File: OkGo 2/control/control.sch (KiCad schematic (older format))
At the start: 49 parts, among them P101 BATT, P102 BATT, P103 BATT_CASE, P104 KEYSW, P105 KEYSW, P106 ARM_LED, P107 ARM_LED, P108 SMA, SW101 LATCHING PUSH, SW102 KEYSWITCH, U101 FUSE 1A, U102 ADP3335, U103 BEZEL, U104 LCD_HD44780, U105 STM32F071CBT6, U106 RFM95W, U107 MEU1S0303ZC, U108 SWD, Y101 8MHz

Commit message: First layout of control
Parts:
- removed TP101: BATT, common:TESTPOINT, symbol TestPoint
- removed TP103: GND, common:TESTPOINT, symbol TestPoint
- removed U101: FUSE 1A, symbol PART
- removed U107: MEU1S0303ZC, control:meu1, symbol MEU1S0303ZC
- added U101: MEJ2S0305SC, control:MEJ2S0305SC, symbol MEJ2S0305SC
- F101: value 5x20 -> PTC; footprint control:5x20_clip -> Resistors_SMD:R_0805; Farnell 1162740 -> 1294879
- U104: footprint Pin_Headers:Pin_Header_Straight_1x16 -> control:LCD_MC42004A6W; Farnell (none) -> 2342651
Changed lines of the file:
@@
 LIBS:adp3335
 LIBS:sma
-LIBS:meu1s0303zc
 LIBS:part
 LIBS:lipo_1s
@@
 LIBS:push_illum
 LIBS:push_illum_straight
+LIBS:mej2s0305sc
 LIBS:control-cache
 EELAYER 25 0
@@
 F 0 "U104" V 8250 3750 60  0000 C CNN
 F 1 "LCD_HD44780" V 8150 3750 60  0000 C CNN
-F 2 "Pin_Headers:Pin_Header_Straight_1x16" H 7450 4400 60  0001 C CNN
+F 2 "control:LCD_MC42004A6W" H 7450 4400 60  0001 C CNN
 F 3 "" H 7450 4400 60  0000 C CNN
+F 4 "2342651" H 8200 3750 60  0001 C CNN "Farnell"
 	1    8200 3750
 	1    0    0    -1
@@
 $EndComp
 $Comp
-L +BATT #PWR023
-U 1 1 55643D33
-P 7150 3550
-F 0 "#PWR023" H 7150 3400 50  0001 C CNN
-F 1 "+BATT" H 7150 3690 50  0000 C CNN
-F 2 "" H 7150 3550 60  0000 C CNN
-F 3 "" H 7150 3550 60  0000 C CNN
-	1    7150 3550
-	1    0    0    -1
-$EndComp
-$Comp
-L GND #PWR024
+L GND #PWR023
 U 1 1 55643E77
 P 7150 3650
-F 0 "#PWR024" H 7150 3400 50  0001 C CNN
+F 0 "#PWR023" H 7150 3400 50  0001 C CNN
 F 1 "GND" H 7150 3500 50  0000 C CNN
 F 2 "" H 7150 3650 60  0000 C CNN
@@
 $EndComp
 $Comp
-L GND #PWR025
+L GND #PWR024
 U 1 1 55638AFF
 P 7100 4150
-F 0 "#PWR025" H 7100 3900 50  0001 C CNN
+F 0 "#PWR024" H 7100 3900 50  0001 C CNN
 F 1 "GND" H 7100 4000 50  0000 C CNN
 F 2 "" H 7100 4150 60  0000 C CNN
@@
 $EndComp
 $Comp
-L TestPoint TP101
-U 1 1 559DAED6
-P 6700 900
-F 0 "TP101" H 6700 825 60  0000 C CNN
-F 1 "BATT" H 6700 750 60  0000 C CNN
-F 2 "common:TESTPOINT" H 6700 900 60  0001 C CNN
-F 3 "" H 6700 900 60  0000 C CNN
-	1    6700 900
-	-1   0    0    1
-$EndComp
-$Comp
-L TestPoint TP103
-U 1 1 559DAFE3
-P 6700 1000
-F 0 "TP103" H 6700 925 60  0000 C CNN
-F 1 "GND" H 6700 850 60  0000 C CNN
-F 2 "common:TESTPOINT" H 6700 1000 60  0001 C CNN
-F 3 "" H 6700 1000 60  0000 C CNN
-	1    6700 1000
-	1    0    0    -1
-$EndComp
-$Comp
 L TestPoint TP104
 U 1 1 559DB26A
@@
 $EndComp
 $Comp
-L GND #PWR026
+L GND #PWR025
 U 1 1 559E503C
 P 9000 5850
-F 0 "#PWR026" H 9000 5600 50  0001 C CNN
+F 0 "#PWR025" H 9000 5600 50  0001 C CNN
 F 1 "GND" H 9000 5700 50  0001 C CNN
 F 2 "" H 9000 5850 60  0000 C CNN
@@
 $EndComp
 $Comp
-L MEU1S0303ZC U107
-U 1 1 559EA3B4
-P 3700 6950
-F 0 "U107" H 3700 6600 60  0000 C CNN
-F 1 "MEU1S0303ZC" H 3750 6900 60  0000 C CNN
-F 2 "control:meu1" H 3700 6950 60  0001 C CNN
-F 3 "" H 3700 6950 60  0000 C CNN
-F 4 "2366449" H 3700 6950 60  0001 C CNN "Farnell"
-	1    3700 6950
-	1    0    0    -1
-$EndComp
-$Comp
-L +3V3 #PWR027
+L +3V3 #PWR026
 U 1 1 559EA6BB
 P 3150 7050
-F 0 "#PWR027" H 3150 6900 50  0001 C CNN
+F 0 "#PWR026" H 3150 6900 50  0001 C CNN
 F 1 "+3V3" H 3150 7190 50  0000 C CNN
 F 2 "" H 3150 7050 60  0000 C CNN
@@
 $EndComp
 $Comp
-L GND #PWR028
+L GND #PWR027
 U 1 1 559EA828
 P 3150 7250
-F 0 "#PWR028" H 3150 7000 50  0001 C CNN
+F 0 "#PWR027" H 3150 7000 50  0001 C CNN
 F 1 "GND" H 3150 7100 50  0000 C CNN
 F 2 "" H 3150 7250 60  0000 C CNN
@@
 $EndComp
 $Comp
-L +5V #PWR029
+L +5V #PWR028
 U 1 1 559EAA6F
 P 4350 7050
-F 0 "#PWR029" H 4350 6900 50  0001 C CNN
+F 0 "#PWR028" H 4350 6900 50  0001 C CNN
 F 1 "+5V" H 4350 7190 50  0000 C CNN
 F 2 "" H 4350 7050 60  0000 C CNN
@@
 $EndComp
 $Comp
-L GND #PWR030
+L GND #PWR029
 U 1 1 559EABE0
 P 4350 7250
-F 0 "#PWR030" H 4350 7000 50  0001 C CNN
+F 0 "#PWR029" H 4350 7000 50  0001 C CNN
 F 1 "GND" H 4350 7100 50  0000 C CNN
 F 2 "" H 4350 7250 60  0000 C CNN
@@
 P 6250 900
 F 0 "F101" H 6350 950 50  0000 C CNN
-F 1 "5x20" H 6150 850 50  0000 C CNN
-F 2 "control:5x20_clip" H 6250 900 60  0001 C CNN
+F 1 "PTC" H 6100 850 50  0000 C CNN
+F 2 "Resistors_SMD:R_0805" H 6250 900 60  0001 C CNN
 F 3 "" H 6250 900 60  0000 C CNN
-F 4 "1162740" H 6250 900 60  0001 C CNN "Farnell"
+F 4 "1294879" H 6250 900 60  0001 C CNN "Farnell"
 	1    6250 900
 	1    0    0    -1
 $EndComp
 $Comp
-L +BATT #PWR031
+L +BATT #PWR030
 U 1 1 55A7EBCE
 P 8300 900
-F 0 "#PWR031" H 8300 750 50  0001 C CNN
+F 0 "#PWR030" H 8300 750 50  0001 C CNN
 F 1 "+BATT" H 8300 1040 50  0000 C CNN
 F 2 "" H 8300 900 60  0000 C CNN
@@
 $EndComp
 $Comp
-L GND #PWR032
+L GND #PWR031
 U 1 1 55A805A4
 P 2000 1550
-F 0 "#PWR032" H 2000 1300 50  0001 C CNN
+F 0 "#PWR031" H 2000 1300 50  0001 C CNN
 F 1 "GND" H 2000 1400 50  0000 C CNN
 F 2 "" H 2000 1550 60  0000 C CNN
@@
 $EndComp
 $Comp
-L +3.3V #PWR033
+L +3.3V #PWR032
 U 1 1 55A80891
 P 2050 1000
-F 0 "#PWR033" H 2050 850 50  0001 C CNN
+F 0 "#PWR032" H 2050 850 50  0001 C CNN
 F 1 "+3.3V" H 2050 1140 50  0000 C CNN
 F 2 "" H 2050 1000 60  0000 C CNN
@@
 	3050 4375 3150 4375
 Connection ~ 10425 950
-Connection ~ 6700 900
-Connection ~ 6700 1000
 Connection ~ 3500 3125
 Wire Wire Line
@@
 Wire Wire Line
 	10650 950  10650 850
-$Comp
-L PART U101
-U 1 1 55AA1AE2
-P 6125 725
-F 0 "U101" H 6250 750 60  0000 C CNN
-F 1 "FUSE 1A" H 6300 825 60  0000 C CNN
-F 2 "" H 6125 725 60  0000 C CNN
-F 3 "" H 6125 725 60  0000 C CNN
-F 4 "FF02178" H 6125 725 60  0001 C CNN "Farnell"
-	1    6125 725
-	1    0    0    -1
-$EndComp
 Wire Wire Line
 	5950 2550 6050 2550
@@
 	5950 2450 6050 2450
 $Comp
-L GND #PWR034
+L GND #PWR033
 U 1 1 55AA7D7E
 P 6050 2700
-F 0 "#PWR034" H 6050 2450 50  0001 C CNN
+F 0 "#PWR033" H 6050 2450 50  0001 C CNN
 F 1 "GND" H 6050 2550 50  0000 C CNN
 F 2 "" H 6050 2700 60  0000 C CNN
@@
 	1    0    0    1
 $EndComp
+$Comp
+L +5V #PWR034
+U 1 1 55AC453D
+P 7150 3550
+F 0 "#PWR034" H 7150 3400 50  0001 C CNN
+F 1 "+5V" H 7150 3690 50  0000 C CNN
+F 2 "" H 7150 3550 60  0000 C CNN
+F 3 "" H 7150 3550 60  0000 C CNN
+	1    7150 3550
+	1    0    0    -1
+$EndComp
+$Comp
+L MEJ2S0305SC U101
+U 1 1 55ACC85A
+P 3700 6950
+F 0 "U101" H 3700 6600 60  0000 C CNN
+F 1 "MEJ2S0305SC" H 3750 6900 60  0000 C CNN
+F 2 "control:MEJ2S0305SC" H 3700 6950 60  0001 C CNN
+F 3 "" H 3700 6950 60  0000 C CNN
+F 4 "2429476" H 3700 6950 60  0001 C CNN "Farnell"
+	1    3700 6950
+	1    0    0    -1
+$EndComp
 $EndSCHEMATC

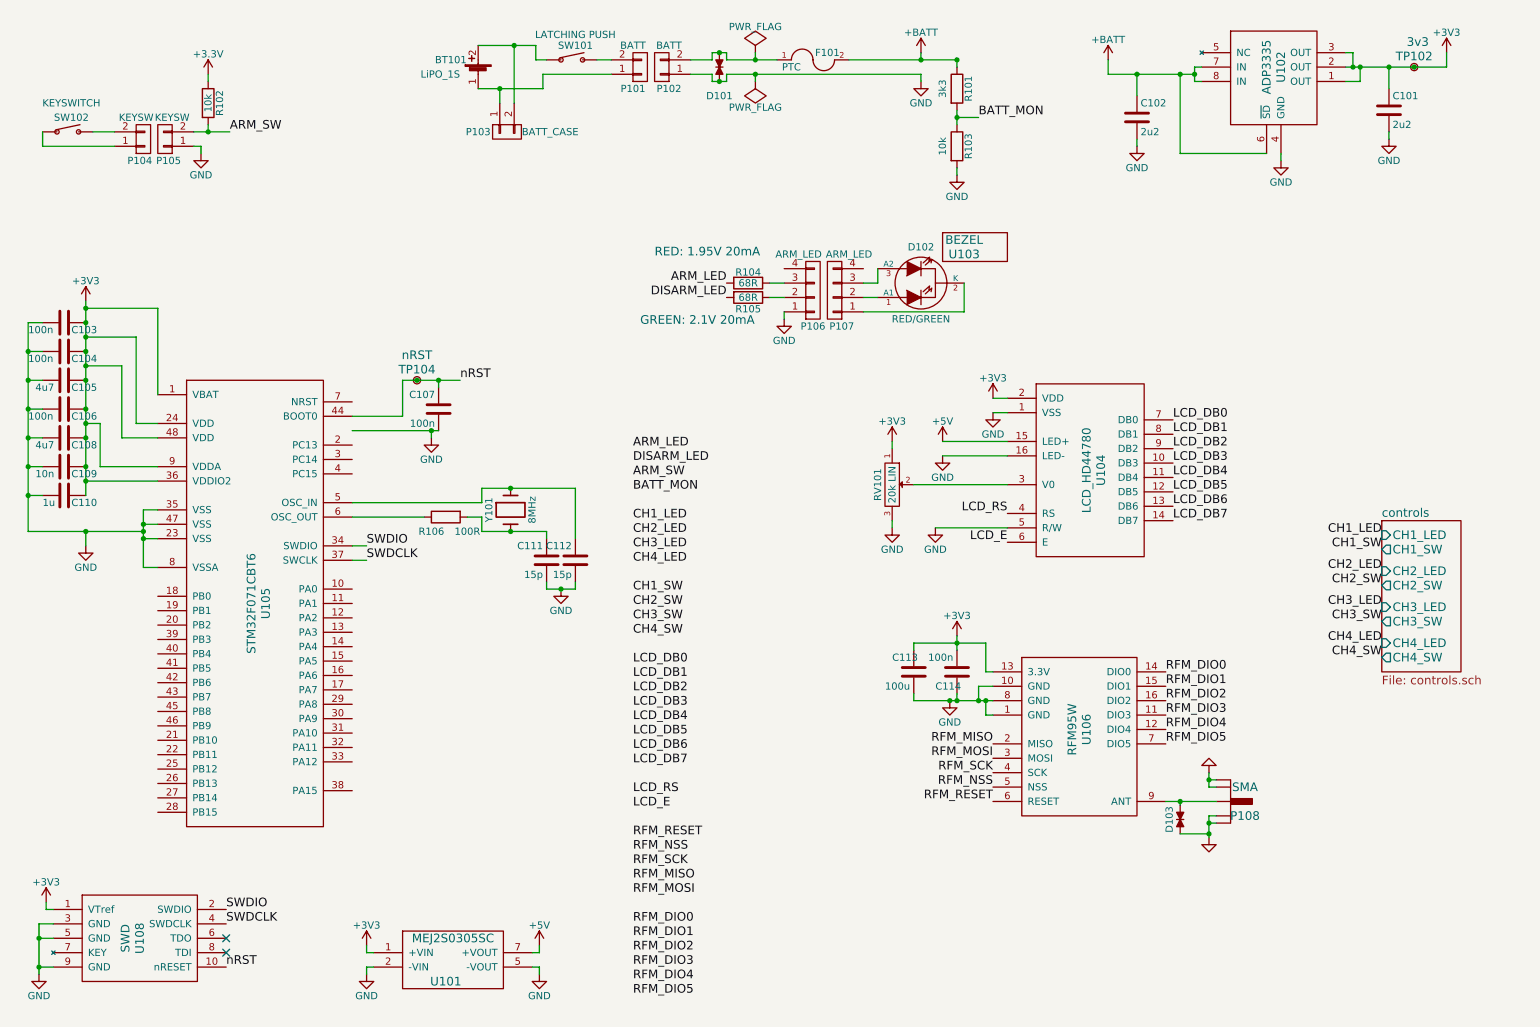
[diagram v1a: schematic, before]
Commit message: 4-bit LCD, pulldowns, 2-pin bicolour ARM LED
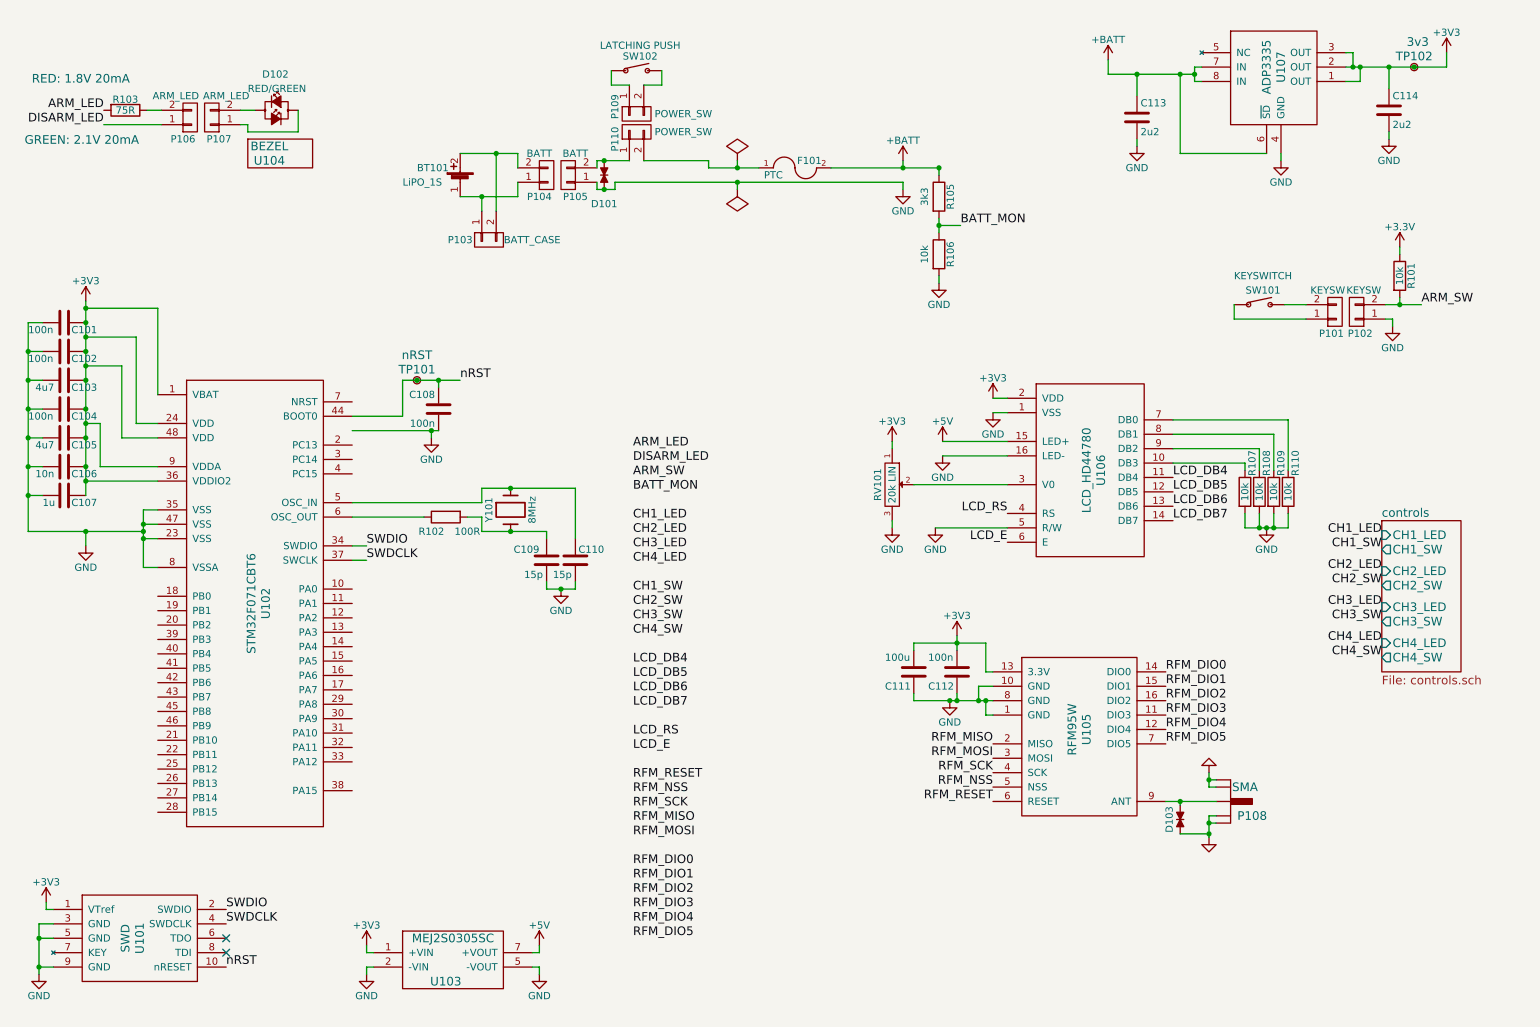
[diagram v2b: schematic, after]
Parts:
- removed D102: RED/GREEN, symbol Led_x2
- removed P106: ARM_LED, common:JST-PA-4, symbol CONN_01X04
- removed P107: ARM_LED, symbol CONN_01X04
- removed R105: 68R, Resistors_SMD:R_0805, symbol R
- added D102: RED/GREEN, symbol LED_bicolour
- added P106: ARM_LED, common:JST-PA-2, symbol CONN_01X02
- added P107: ARM_LED, symbol CONN_01X02
- added P109: POWER_SW, symbol CONN_01X02
- added P110: POWER_SW, common:JST-PA-2, symbol CONN_01X02
- added R107, R108, R109, R110: 10k, Resistors_SMD:R_0805, symbol R
- P103: footprint common:JST-PA-2 -> (none)
- R103: renamed from R104; value 68R -> 75R; Farnell 2332055 -> 2331781
- renumbered C103 to C101, C104 to C102, C105 to C103, C106 to C104, C108 to C105, C109 to C106, C110 to C107, C107 to C108, C111 to C109, C112 to C110, C113 to C111, C114 to C112, C102 to C113, C101 to C114, P104 to P101, P105 to P102, P101 to P104, P102 to P105, R102 to R101, R106 to R102, R101 to R105, R103 to R106, SW102 to SW101, SW101 to SW102, TP104 to TP101, U108 to U101, U105 to U102, U101 to U103, U103 to U104, U106 to U105, U104 to U106, U102 to U107
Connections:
- net +3V3: now also C111.2; no longer C111.1
- net DISARM_LED: now also P106.1 (P1)
- net GND: now also C111.1, R107.2, R108.2, R109.2, R110.2; no longer C111.2
- net at D101.1, P105.2 (P2): now also P110.1 (P1); no longer F101.1
- net at BT101.2, P103.2 (P2): now also P104.2 (P2); no longer SW102.1
- net at SW102.2: now also P109.2 (P2); no longer P104.2 (P2)
- net at R103.1: now also P106.2 (P2)
- net LCD_DB0: no longer names the net of U106.7 (DB0)
- net LCD_DB0: now also R110.1
- net LCD_DB1: no longer names the net of U106.8 (DB1)
- net LCD_DB1: now also R109.1
- net LCD_DB2: no longer names the net of U106.9 (DB2)
- net LCD_DB2: now also R108.1
- net LCD_DB3: no longer names the net of U106.10 (DB3)
- net LCD_DB3: now also R107.1
- new net: F101.1, P110.2 (P2)
- new net: P109.1 (P1), SW102.1
- new net: D102.2 (A), P107.1 (P1)
- new net: D102.1 (K), P107.2 (P2)
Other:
- note added: "RED: 1.8V 20mA"
- note removed: "RED: 1.95V 20mA"
- moved on the sheet: BT101, D101, F101, P101, P102, P103, P104, P105, R101, R103, R105, R106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

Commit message: Finished demo-route of control
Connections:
- net ARM_LED: now also U102.29 (PA8)
- net ARM_SW: now also U102.31 (PA10)
- net BATT_MON: now also U102.19 (PB1)
- net CH1_LED: now also U102.18 (PB0)
- net CH1_SW: now also U102.20 (PB2)
- net CH2_LED: now also U102.21 (PB10)
- net CH2_SW: now also U102.22 (PB11)
- net CH3_LED: now also U102.25 (PB12)
- net CH3_SW: now also U102.26 (PB13)
- net CH4_LED: now also U102.27 (PB14)
- net CH4_SW: now also U102.28 (PB15)
- net DISARM_LED: now also U102.30 (PA9)
- net GND: now also U102.44 (BOOT0)
- net LCD_DB4: now also U102.42 (PB6)
- net LCD_DB5: now also U102.43 (PB7)
- net LCD_DB6: now also U102.45 (PB8)
- net LCD_DB7: now also U102.46 (PB9)
- net LCD_E: now also U102.39 (PB3)
- net LCD_RS: now also U102.38 (PA15)
- net RFM_DIO0: now also U102.4 (PC15)
- net RFM_DIO1: now also U102.10 (PA0)
- net RFM_DIO2: now also U102.11 (PA1)
- net RFM_DIO3: now also U102.2 (PC13)
- net RFM_DIO4: now also U102.3 (PC14)
- net RFM_DIO5: now also U102.12 (PA2)
- net RFM_MISO: now also U102.16 (PA6)
- net RFM_MOSI: now also U102.17 (PA7)
- net RFM_NSS: now also U102.14 (PA4)
- net RFM_RESET: now also U102.13 (PA3)
- net RFM_SCK: now also U102.15 (PA5)
- net nRST: now also U102.7 (NRST); no longer U102.44 (BOOT0)
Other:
- moved on the sheet: C108, TP101
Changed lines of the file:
@@
 L C C108
 U 1 1 5562E486
-P 3650 3325
-F 0 "C108" H 3675 3425 50  0000 L CNN
-F 1 "100n" H 3675 3225 50  0000 L CNN
-F 2 "Capacitors_SMD:C_0805" H 3688 3175 30  0001 C CNN
-F 3 "" H 3650 3325 60  0000 C CNN
-F 4 "2407344" H 3650 3325 60  0001 C CNN "Farnell"
-	1    3650 3325
+P 3650 3225
+F 0 "C108" H 3675 3325 50  0000 L CNN
+F 1 "100n" H 3675 3125 50  0000 L CNN
+F 2 "Capacitors_SMD:C_0805" H 3688 3075 30  0001 C CNN
+F 3 "" H 3650 3225 60  0000 C CNN
+F 4 "2407344" H 3650 3225 60  0001 C CNN "Farnell"
+	1    3650 3225
 	-1   0    0    -1
 $EndComp
@@
 L GND #PWR014
 U 1 1 5562E73A
-P 3600 3525
-F 0 "#PWR014" H 3600 3275 50  0001 C CNN
-F 1 "GND" H 3600 3375 50  0000 C CNN
-F 2 "" H 3600 3525 60  0000 C CNN
-F 3 "" H 3600 3525 60  0000 C CNN
-	1    3600 3525
+P 3600 3425
+F 0 "#PWR014" H 3600 3175 50  0001 C CNN
+F 1 "GND" H 3600 3275 50  0000 C CNN
+F 2 "" H 3600 3425 60  0000 C CNN
+F 3 "" H 3600 3425 60  0000 C CNN
+	1    3600 3425
 	-1   0    0    -1
 $EndComp
@@
 	0    -1   -1   0
 $EndComp
-Text Label 3800 3125 0    60   ~ 0
+Text Label 3800 3025 0    60   ~ 0
 nRST
 Text Label 3150 4275 0    60   ~ 0
@@
 Text Label 7500 6050 2    60   ~ 0
 RFM_RESET
-Text Label 5000 6500 0    60   ~ 0
+Text Label 3050 3775 0    60   ~ 0
 RFM_DIO0
-Text Label 5000 6600 0    60   ~ 0
+Text Label 3050 4575 0    60   ~ 0
 RFM_DIO1
-Text Label 5000 6700 0    60   ~ 0
+Text Label 3050 4675 0    60   ~ 0
 RFM_DIO2
-Text Label 5000 6800 0    60   ~ 0
+Text Label 3050 3575 0    60   ~ 0
 RFM_DIO3
-Text Label 5000 6900 0    60   ~ 0
+Text Label 3050 3675 0    60   ~ 0
 RFM_DIO4
-Text Label 5000 7000 0    60   ~ 0
+Text Label 3050 4775 0    60   ~ 0
 RFM_DIO5
-Text Label 5000 6000 0    60   ~ 0
+Text Label 3050 4975 0    60   ~ 0
 RFM_NSS
-Text Label 5000 6100 0    60   ~ 0
+Text Label 3050 5075 0    60   ~ 0
 RFM_SCK
-Text Label 5000 6200 0    60   ~ 0
+Text Label 3050 5175 0    60   ~ 0
 RFM_MISO
-Text Label 5000 6300 0    60   ~ 0
+Text Label 3050 5275 0    60   ~ 0
 RFM_MOSI
 Text Label 8750 3800 0    60   ~ 0
@@
 Text Label 7275 2050 0    60   ~ 0
 BATT_MON
-Text Label 5000 4600 0    60   ~ 0
+Text Label 1700 4825 2    60   ~ 0
 CH1_SW
-Text Label 5000 4700 0    60   ~ 0
+Text Label 1700 5725 2    60   ~ 0
 CH2_SW
-Text Label 5000 4800 0    60   ~ 0
+Text Label 1700 5925 2    60   ~ 0
 CH3_SW
-Text Label 5000 4900 0    60   ~ 0
+Text Label 1700 6125 2    60   ~ 0
 CH4_SW
-Text Label 5000 4100 0    60   ~ 0
+Text Label 1700 4625 2    60   ~ 0
 CH1_LED
-Text Label 5000 4200 0    60   ~ 0
+Text Label 1700 5625 2    60   ~ 0
 CH2_LED
-Text Label 5000 4300 0    60   ~ 0
+Text Label 1700 5825 2    60   ~ 0
 CH3_LED
-Text Label 5000 4400 0    60   ~ 0
+Text Label 1700 6025 2    60   ~ 0
 CH4_LED
-Text Label 5000 5900 0    60   ~ 0
+Text Label 3050 4875 0    60   ~ 0
 RFM_RESET
-Text Label 5000 5100 0    60   ~ 0
+Text Label 1700 5225 2    60   ~ 0
 LCD_DB4
-Text Label 5000 5200 0    60   ~ 0
+Text Label 1700 5325 2    60   ~ 0
 LCD_DB5
-Text Label 5000 5300 0    60   ~ 0
+Text Label 1700 5425 2    60   ~ 0
 LCD_DB6
-Text Label 5000 5400 0    60   ~ 0
+Text Label 1700 5525 2    60   ~ 0
 LCD_DB7
-Text Label 5000 5600 0    60   ~ 0
+Text Label 3050 5975 0    60   ~ 0
 LCD_RS
-Text Label 5000 5700 0    60   ~ 0
+Text Label 1700 4925 2    60   ~ 0
 LCD_E
-Text Label 5000 3900 0    60   ~ 0
+Text Label 1700 4725 2    60   ~ 0
 BATT_MON
 $Comp
@@
 L TestPoint TP101
 U 1 1 559DB26A
-P 3500 3125
-F 0 "TP101" H 3500 3050 60  0000 C CNN
-F 1 "nRST" H 3500 2950 60  0000 C CNN
-F 2 "common:TESTPOINT" H 3500 3125 60  0001 C CNN
-F 3 "" H 3500 3125 60  0000 C CNN
-	1    3500 3125
+P 3500 3025
+F 0 "TP101" H 3500 2950 60  0000 C CNN
+F 1 "nRST" H 3500 2850 60  0000 C CNN
+F 2 "common:TESTPOINT" H 3500 3025 60  0001 C CNN
+F 3 "" H 3500 3025 60  0000 C CNN
+	1    3500 3025
 	-1   0    0    1
 $EndComp
@@
 Connection ~ 1600 4175
 Wire Wire Line
-	3650 3125 3650 3175
-Connection ~ 3650 3125
-Wire Wire Line
-	3050 3475 3650 3475
-Wire Wire Line
-	3600 3475 3600 3525
-Wire Wire Line
-	3400 3125 3800 3125
-Wire Wire Line
-	3400 3375 3050 3375
+	3650 3025 3650 3075
+Connection ~ 3650 3025
+Wire Wire Line
+	3050 3375 3650 3375
+Wire Wire Line
+	3600 3375 3600 3425
+Wire Wire Line
+	3400 3025 3800 3025
+Wire Wire Line
+	3400 3275 3050 3275
 Wire Wire Line
 	3050 3975 3950 3975
@@
 	7100 4150 7600 4150
 Wire Wire Line
-	3400 3125 3400 3375
-Connection ~ 3600 3475
+	3400 3025 3400 3275
+Connection ~ 3600 3375
 Wire Wire Line
 	4750 1650 4750 1600
@@
 	3050 4375 3150 4375
 Connection ~ 10425 950
-Connection ~ 3500 3125
+Connection ~ 3500 3025
 Wire Wire Line
 	3050 4075 3550 4075
@@
 	0    1    1    0
 $EndComp
-Text Label 5000 3800 0    60   ~ 0
+Text Label 3050 5575 0    60   ~ 0
 ARM_SW
-Text Label 5000 3700 0    60   ~ 0
+Text Label 3050 5475 0    60   ~ 0
 DISARM_LED
-Text Label 5000 3600 0    60   ~ 0
+Text Label 3050 5375 0    60   ~ 0
 ARM_LED
 $Comp
